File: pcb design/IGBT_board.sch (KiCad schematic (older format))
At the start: 53 parts, among them J1 4-794627-0, Q1 IGBT, Q10 IGBT, Q11 IGBT, Q12 IGBT, Q2 IGBT, Q3 IGBT, Q4 IGBT, Q5 IGBT, Q6 IGBT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

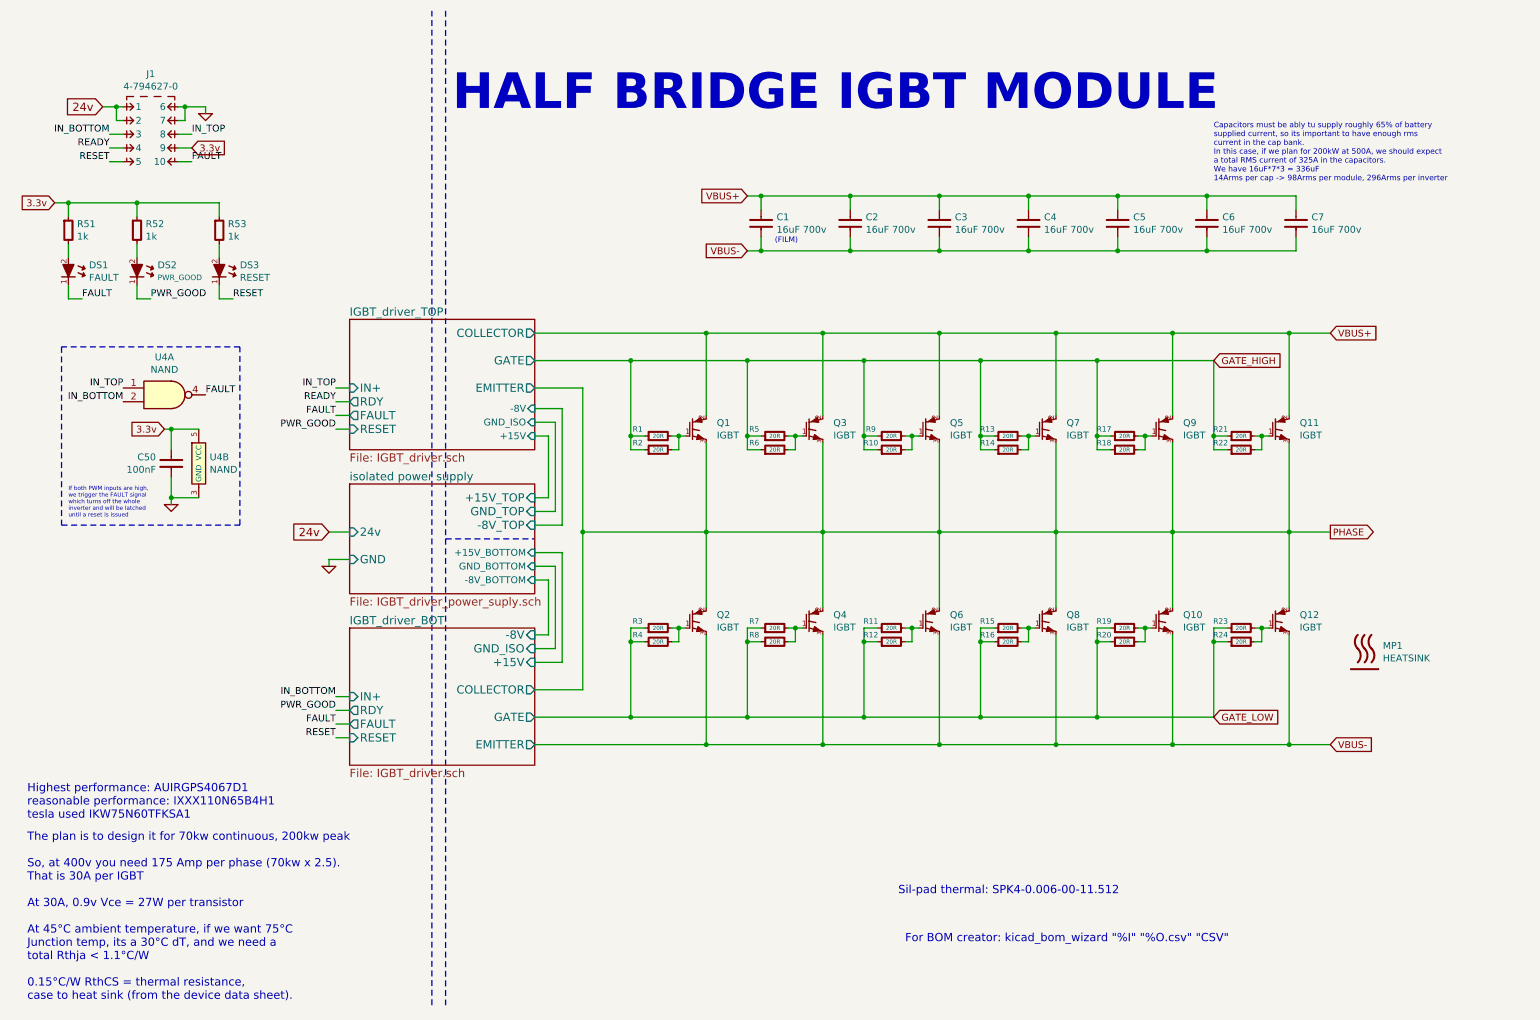
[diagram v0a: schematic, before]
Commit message: Added on board 3.3v regulator, power supply fuse and some resistors to protect digital lines
Signed-off-by: Marcos Chaparro <mchaparro@paltatech.com>
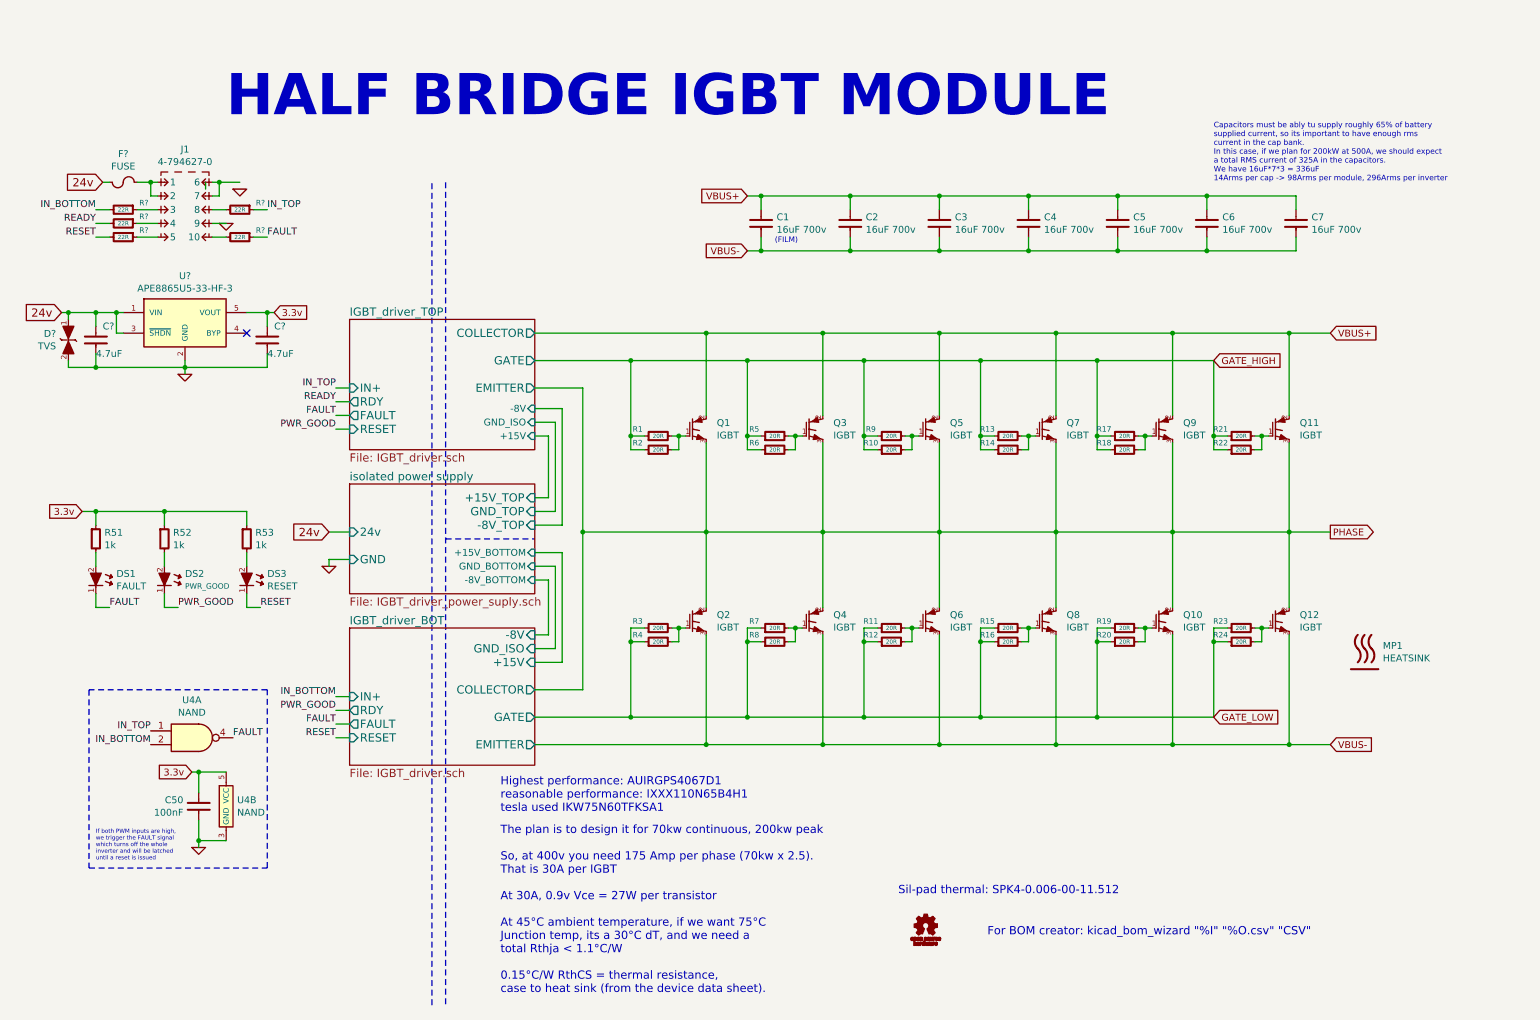
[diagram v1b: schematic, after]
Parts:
- added C? (x2): 4.7uF, IPC7351-Nominal:CAPC2012X70, symbol C-0805
- added D?: TVS, Diodes_SMD:Diode-SMB_Standard, symbol TVS_BI
- added F?: FUSE, IPC7351-Nominal:RESC3216X60, symbol FUSE
- added R? (x5): 22R, IPC7351-Nominal:RESC1608X50, symbol R-0603
- added SYM?: OSHW-SCHEM-PCB10mm, mech:OSHW-10mm, symbol OSHW-SCHEM-PCB10mm
- added U?: APE8865U5-33-HF-3, SC-70-5, symbol APE8865U5-33-HF-3
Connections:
- net 24v: now also C?.1, D?.1 (A1), F?.1, U?.1 (VIN), U?.3 (~SHDN~); no longer J1.1, J1.2
- net 3.3v: now also C?.1, U?.5 (VOUT); no longer J1.9
- net FAULT: now also R?.1; no longer J1.10
- net GND: now also J1.9, C?.2, C?.2, D?.2 (A2), U?.2 (GND); no longer J1.6, J1.7
- net IN_BOTTOM: now also R?.2; no longer J1.3
- net IN_TOP: now also R?.1; no longer J1.8
- net READY: now also R?.2; no longer J1.4
- net RESET: now also R?.2; no longer J1.5
- new net: F?.2, J1.1, J1.2
- new net: J1.10, R?.2
- new net: J1.3, R?.1
- new net: J1.4, R?.1
- new net: J1.5, R?.1
- new net: J1.6, J1.7
- new net: J1.8, R?.2
- no-connect marks 0 -> 1
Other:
- moved on the sheet: C50, DS1, DS2, DS3, J1, R51, R52, R53, U4A, U4B

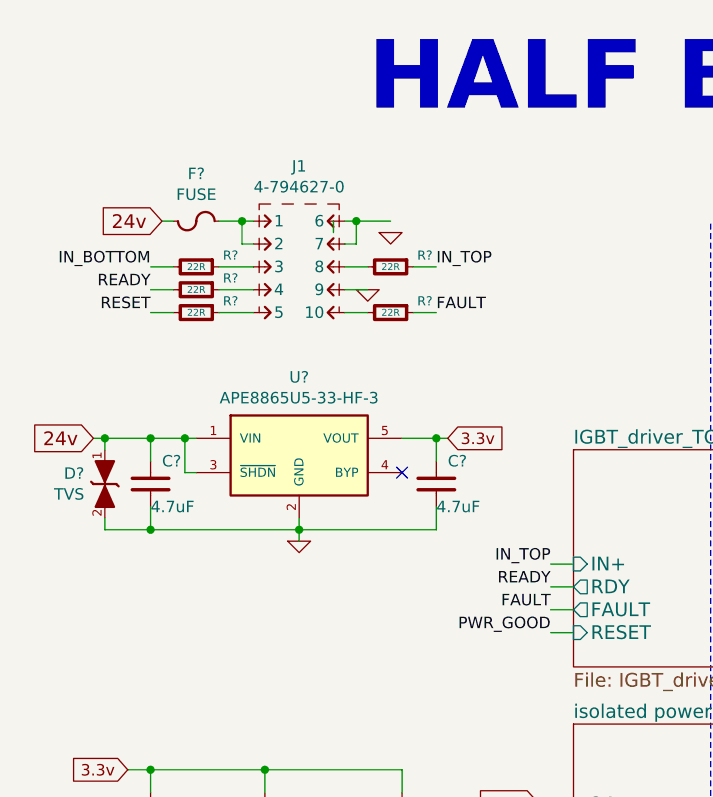
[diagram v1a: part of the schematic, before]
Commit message: Fixed schematic label and more layout
Signed-off-by: Marcos Chaparro <mchaparro@paltatech.com>
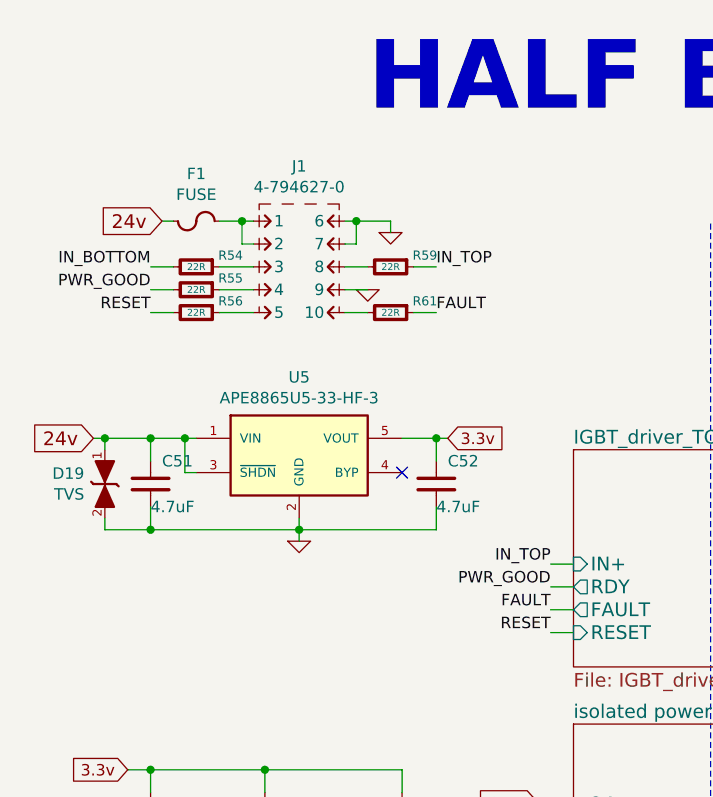
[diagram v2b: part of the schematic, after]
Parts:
- SYM1: renamed from SYM?; footprint mech:OSHW-10mm -> w_logo:Logo_silk_OSHW_12x13mm
- gave numbers to parts that had none: 10
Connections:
- net READY is gone; now on net PWR_GOOD: R55.2
- net GND: now also J1.6, J1.7
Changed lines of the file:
@@
 Text Label 2850 3250 2    50   ~ 0
 IN_TOP
-Text Label 2850 3350 2    50   ~ 0
-READY
 Text Label 2850 3450 2    50   ~ 0
 FAULT
-Text Label 2850 3550 2    50   ~ 0
+Text Label 2850 3350 2    50   ~ 0
 PWR_GOOD
 Text Label 2850 5500 2    50   ~ 0
@@
 Text Label 2350 1950 0    50   ~ 0
 IN_TOP
-Text Label 1100 2050 2    50   ~ 0
-READY
 Text Label 2350 2150 0    50   ~ 0
 FAULT
@@
 3.3v
 $Comp
-L FUSE F?
+L FUSE F1
 U 1 1 583A1221
 P 1300 1750
-F 0 "F?" V 1507 1750 50  0000 C CNN
+F 0 "F1" V 1507 1750 50  0000 C CNN
 F 1 "FUSE" V 1416 1750 50  0000 C CNN
 F 2 "IPC7351-Nominal:RESC3216X60" V 1423 1750 60  0001 C CNN
@@
 $EndComp
 $Comp
-L TVS_BI D?
+L TVS_BI D19
 U 1 1 583A5A92
 P 900 2900
-F 0 "D?" H 990 2946 50  0000 L CNN
+F 0 "D19" H 990 2946 50  0000 L CNN
 F 1 "TVS" H 990 2855 50  0000 L CNN
 F 2 "Diodes_SMD:Diode-SMB_Standard" H 900 2950 60  0001 C CNN
@@
 $EndComp
 $Comp
-L C-0805 C?
+L C-0805 C51
 U 1 1 583A623D
 P 1100 2900
-F 0 "C?" H 1150 3000 50  0000 L CNN
+F 0 "C51" H 1150 3000 50  0000 L CNN
 F 1 "4.7uF" H 1100 2800 50  0000 L CNN
 F 2 "IPC7351-Nominal:CAPC2012X70" H 1100 2900 50  0001 C CNN
@@
 $EndComp
 $Comp
-L APE8865U5-33-HF-3 U?
+L APE8865U5-33-HF-3 U5
 U 1 1 583A7253
 P 1750 2750
-F 0 "U?" H 1750 3067 50  0000 C CNN
+F 0 "U5" H 1750 3067 50  0000 C CNN
 F 1 "APE8865U5-33-HF-3" H 1750 2976 50  0000 C CNN
 F 2 "SC-70-5" H 1750 2976 50  0001 C CIN
@@
 $EndComp
 $Comp
-L C-0805 C?
+L C-0805 C52
 U 1 1 583A9014
 P 2350 2900
-F 0 "C?" H 2400 3000 50  0000 L CNN
+F 0 "C52" H 2400 3000 50  0000 L CNN
 F 1 "4.7uF" H 2350 2800 50  0000 L CNN
 F 2 "IPC7351-Nominal:CAPC2012X70" H 2350 2900 50  0001 C CNN
@@
 Connection ~ 1500 1750
 Wire Wire Line
-	1900 1750 1900 1800
-Wire Wire Line
 	1950 1750 2150 1750
 Wire Wire Line
@@
 Connection ~ 2350 2700
 $Comp
-L GND #PWR?
+L GND #PWR04
 U 1 1 583AB791
 P 1750 3150
-F 0 "#PWR?" H 1750 3150 30  0001 C CNN
+F 0 "#PWR04" H 1750 3150 30  0001 C CNN
 F 1 "GND" H 1750 3080 30  0001 C CNN
 F 2 "" H 1750 3150 60  0000 C CNN
@@
 $EndComp
 $Comp
-L GND #PWR?
+L GND #PWR05
 U 1 1 583AF86E
 P 2050 2050
-F 0 "#PWR?" H 2050 2050 30  0001 C CNN
+F 0 "#PWR05" H 2050 2050 30  0001 C CNN
 F 1 "GND" H 2050 1980 30  0001 C CNN
 F 2 "" H 2050 2050 60  0000 C CNN
@@
 $EndComp
 $Comp
-L OSHW-SCHEM-PCB10mm SYM?
+L OSHW-SCHEM-PCB10mm SYM1
 U 1 1 583B5122
 P 7150 7200
-F 0 "SYM?" H 7284 7200 50  0001 L CNN
+F 0 "SYM1" H 7284 7200 50  0001 L CNN
 F 1 "OSHW-SCHEM-PCB10mm" H 7150 7150 50  0001 C CNN
-F 2 "mech:OSHW-10mm" H 7200 7100 50  0001 C CNN
+F 2 "w_logo:Logo_silk_OSHW_12x13mm" H 7200 7100 50  0001 C CNN
 F 3 "" H 7150 7200 50  0000 C CNN
 	1    7150 7200
@@
 $EndComp
 $Comp
-L R-0603 R?
+L R-0603 R54
 U 1 1 583B7739
 P 1300 1950
-F 0 "R?" V 1250 2100 40  0000 C CNN
+F 0 "R54" V 1250 2100 40  0000 C CNN
 F 1 "22R" V 1300 1950 30  0000 C CNN
 F 2 "IPC7351-Nominal:RESC1608X50" H 1300 1950 50  0001 C CNN
@@
 $EndComp
 $Comp
-L R-0603 R?
+L R-0603 R55
 U 1 1 583B8694
 P 1300 2050
-F 0 "R?" V 1250 2200 40  0000 C CNN
+F 0 "R55" V 1250 2200 40  0000 C CNN
 F 1 "22R" V 1300 2050 30  0000 C CNN
 F 2 "IPC7351-Nominal:RESC1608X50" H 1300 2050 50  0001 C CNN
@@
 $EndComp
 $Comp
-L R-0603 R?
+L R-0603 R56
 U 1 1 583B8848
 P 1300 2150
-F 0 "R?" V 1250 2300 40  0000 C CNN
+F 0 "R56" V 1250 2300 40  0000 C CNN
 F 1 "22R" V 1300 2150 30  0000 C CNN
 F 2 "IPC7351-Nominal:RESC1608X50" H 1300 2150 50  0001 C CNN
@@
 	1200 1950 1100 1950
 $Comp
-L R-0603 R?
+L R-0603 R59
 U 1 1 583B9B4D
 P 2150 1950
-F 0 "R?" V 2100 2100 40  0000 C CNN
+F 0 "R59" V 2100 2100 40  0000 C CNN
 F 1 "22R" V 2150 1950 30  0000 C CNN
 F 2 "IPC7351-Nominal:RESC1608X50" H 2150 1950 50  0001 C CNN
@@
 	2350 1950 2250 1950
 $Comp
-L R-0603 R?
+L R-0603 R61
 U 1 1 583B9E90
 P 2150 2150
-F 0 "R?" V 2100 2300 40  0000 C CNN
+F 0 "R61" V 2100 2300 40  0000 C CNN
 F 1 "22R" V 2150 2150 30  0000 C CNN
 F 2 "IPC7351-Nominal:RESC1608X50" H 2150 2150 50  0001 C CNN
@@
 Wire Notes Line
 	3550 7750 3550 1750
+Wire Wire Line
+	2150 1750 2150 1800
+Text Label 2850 3550 2    50   ~ 0
+RESET
+Text Label 1100 2050 2    50   ~ 0
+PWR_GOOD
 $EndSCHEMATC
